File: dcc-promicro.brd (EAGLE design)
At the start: 33 x 17.8 mm, 7 parts, among them Q1 MOSFET-NCHANNEL2N7002PW

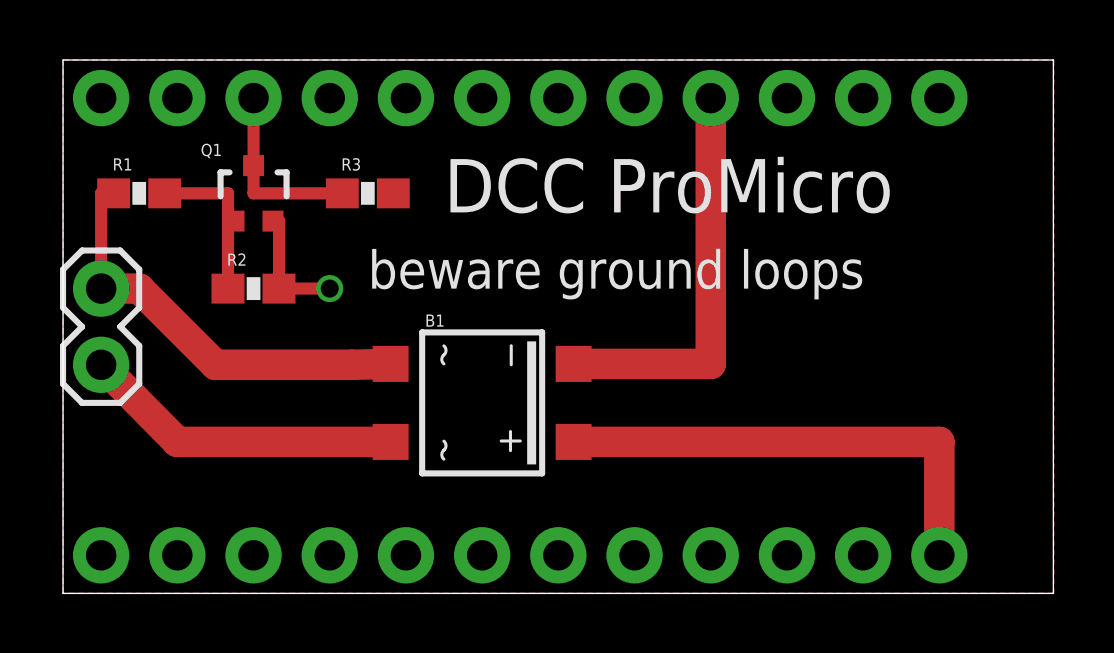
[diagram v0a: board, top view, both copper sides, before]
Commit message: add a-star variant, use JST for dcc-powered boards
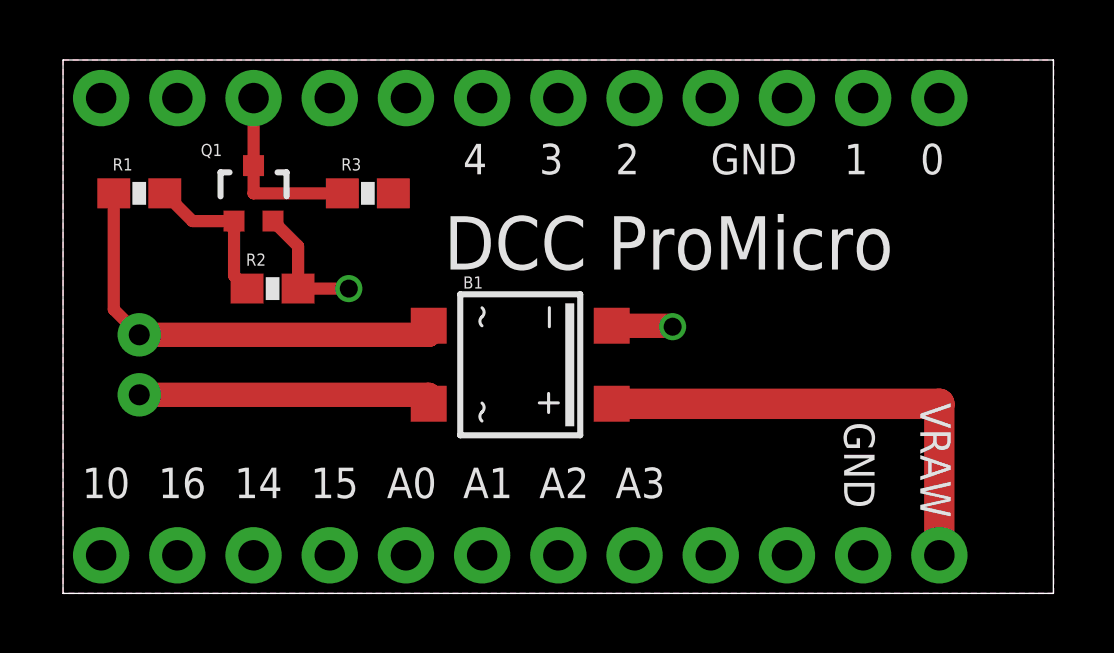
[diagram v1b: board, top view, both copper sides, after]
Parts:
- DCC-IN: value M02PTH -> M02-JST-2-PTH-NO_SILK; device SparkFun-Connectors:1X02 -> SparkFun-Connectors:JST-2-PTH-NS
- moved B1 1.80 mm to (15.2, 7.62)
- moved DCC-IN 1.27 mm to (2.54, 7.62)
- moved R2 0.64 mm to (6.99, 10.2)
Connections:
- net GND: now also U$1.23
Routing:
- net GND: track 17.6 -> 6.35 mm, vias 1 -> 2
- net N$4: track 10.8 -> 9.95 mm
- net N$3: track 14.3 -> 15.0 mm
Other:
- board text added: "0"
- board text added: "1"
- board text added: "10"
- board text added: "14"
- board text added: "15"
- board text added: "16"
- board text added: "2"
- board text added: "3"
- board text added: "4"
- board text added: "A0"
- board text added: "A1"
- board text added: "A2"
- board text added: "A3"
- board text added: "GND"
- board text added: "VRAW"
- board text removed: "beware ground loops"
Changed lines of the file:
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@@
 <layers>
 <layer number="1" name="Top" color="4" fill="1" visible="yes" active="yes"/>
+<layer number="2" name="Route2" color="1" fill="3" visible="no" active="no"/>
+<layer number="3" name="Route3" color="4" fill="3" visible="no" active="no"/>
+<layer number="14" name="Route14" color="1" fill="6" visible="no" active="no"/>
+<layer number="15" name="Route15" color="4" fill="6" visible="no" active="no"/>
 <layer number="16" name="Bottom" color="1" fill="1" visible="yes" active="yes"/>
 <layer number="17" name="Pads" color="2" fill="1" visible="yes" active="yes"/>
@@
 <wire x1="33.01" y1="0" x2="33.01" y2="17.78" width="0" layer="20"/>
 <wire x1="33.01" y1="17.78" x2="0" y2="17.78" width="0" layer="20"/>
-<text x="12.7" y="12.7" size="1.778" layer="21" font="vector">DCC ProMicro</text>
-<text x="10.16" y="10.16" size="1.27" layer="21" font="vector">beware ground loops</text>
+<text x="12.7" y="10.795" size="1.778" layer="21" font="vector">DCC ProMicro</text>
+<text x="13.335" y="13.97" size="1.016" layer="21">4</text>
+<text x="18.415" y="13.97" size="1.016" layer="21">2</text>
+<text x="15.875" y="13.97" size="1.016" layer="21">3</text>
+<text x="0.635" y="3.175" size="1.016" layer="21" rot="SR0">10</text>
+<text x="3.175" y="3.175" size="1.016" layer="21">16</text>
+<text x="5.715" y="3.175" size="1.016" layer="21">14</text>
+<text x="8.255" y="3.175" size="1.016" layer="21">15</text>
+<text x="26.035" y="13.97" size="1.016" layer="21">1</text>
+<text x="28.575" y="13.97" size="1.016" layer="21">0</text>
+<text x="21.59" y="13.97" size="1.016" layer="21">GND</text>
+<text x="28.575" y="6.35" size="1.016" layer="21" rot="SR270">VRAW</text>
+<text x="10.795" y="3.175" size="1.016" layer="21">A0</text>
+<text x="13.335" y="3.175" size="1.016" layer="21">A1</text>
+<text x="15.875" y="3.175" size="1.016" layer="21" rot="SR0">A2</text>
+<text x="18.415" y="3.175" size="1.016" layer="21" rot="SR0">A3</text>
+<text x="26.035" y="5.715" size="1.016" layer="21" rot="SR270">GND</text>
 </plain>
 <attributes>
@@
 </autorouter>
 <elements>
-<element name="DCC-IN" library="SparkFun-Connectors" package="1X02" value="M02PTH" x="1.27" y="7.62" smashed="yes" rot="R90"/>
+<element name="DCC-IN" library="SparkFun-Connectors" package="JST-2-PTH-NS" value="M02-JST-2-PTH-NO_SILK" x="2.54" y="7.62" smashed="yes" rot="R90"/>
 <element name="U$1" library="SparkFun-Boards" package="ARDUINO_PRO_MICRO" value="ARDUINO_PRO_MICRO" x="16.51" y="8.89" smashed="yes" rot="R270"/>
-<element name="B1" library="rectifier" package="SOIC-4" value="MB1S" x="13.97" y="6.35" smashed="yes" rot="R270">
-<attribute name="NAME" x="12.065" y="8.89" size="0.4064" layer="25"/>
+<element name="B1" library="rectifier" package="SOIC-4" value="MB1S" x="15.24" y="7.62" smashed="yes" rot="R270">
+<attribute name="NAME" x="13.335" y="10.16" size="0.4064" layer="25"/>
 </element>
 <element name="R1" library="SparkFun-Passives" package="0603-RES" value="47K" x="2.54" y="13.335"/>
@@
 </element>
 <element name="R3" library="SparkFun-Passives" package="0603-RES" value="10K" x="10.16" y="13.335"/>
-<element name="R2" library="SparkFun-Passives" package="0603-RES" value="100K" x="6.35" y="10.16"/>
+<element name="R2" library="SparkFun-Passives" package="0603-RES" value="100K" x="6.985" y="10.16"/>
 </elements>
 <signals>
@@
 <contactref element="B1" pad="-"/>
 <contactref element="Q1" pad="2"/>
-<wire x1="21.59" y1="16.51" x2="21.59" y2="7.65" width="1.016" layer="1"/>
-<wire x1="21.59" y1="7.65" x2="17.02" y2="7.65" width="1.016" layer="1"/>
 <contactref element="R2" pad="2"/>
-<wire x1="7.2" y1="10.16" x2="7.2" y2="12.41" width="0.4064" layer="1"/>
-<wire x1="7.2" y1="12.41" x2="7" y2="12.41" width="0.4064" layer="1"/>
-<wire x1="7.2" y1="10.16" x2="8.89" y2="10.16" width="0.4064" layer="1"/>
-<via x="8.89" y="10.16" extent="1-16" drill="0.6" shape="square"/>
+<wire x1="7.835" y1="10.16" x2="9.525" y2="10.16" width="0.4064" layer="1"/>
+<via x="9.525" y="10.16" extent="1-16" drill="0.6" shape="square"/>
+<contactref element="U$1" pad="23"/>
+<wire x1="18.29" y1="8.92" x2="20.32" y2="8.92" width="0.8128" layer="1"/>
+<wire x1="20.32" y1="8.92" x2="20.32" y2="8.89" width="0.8128" layer="1"/>
+<via x="20.32" y="8.89" extent="1-16" drill="0.6" shape="square"/>
+<wire x1="7.835" y1="10.16" x2="7.835" y2="11.575" width="0.4064" layer="1"/>
+<wire x1="7.835" y1="11.575" x2="7" y2="12.41" width="0.4064" layer="1"/>
 </signal>
 <signal name="DCC-INT">
@@
 <contactref element="U$1" pad="24"/>
 <contactref element="B1" pad="+"/>
-<wire x1="17.02" y1="5.05" x2="29.21" y2="5.05" width="1.016" layer="1"/>
-<wire x1="29.21" y1="5.05" x2="29.21" y2="1.27" width="1.016" layer="1"/>
+<wire x1="18.29" y1="6.32" x2="29.21" y2="6.32" width="1.016" layer="1"/>
+<wire x1="29.21" y1="6.32" x2="29.21" y2="1.27" width="1.016" layer="1"/>
 </signal>
 <signal name="N$3">
@@
 <contactref element="DCC-IN" pad="2"/>
 <contactref element="R1" pad="1"/>
-<wire x1="1.27" y1="10.16" x2="2.54" y2="10.16" width="1.016" layer="1"/>
-<wire x1="2.54" y1="10.16" x2="5.08" y2="7.62" width="1.016" layer="1"/>
-<wire x1="5.08" y1="7.62" x2="9.62" y2="7.62" width="1.016" layer="1"/>
-<wire x1="9.62" y1="7.62" x2="10.92" y2="7.65" width="1.016" layer="1"/>
-<wire x1="1.27" y1="10.16" x2="1.27" y2="13.335" width="0.4064" layer="1"/>
-<wire x1="1.27" y1="13.335" x2="1.69" y2="13.335" width="0.4064" layer="1"/>
+<wire x1="2.54" y1="8.62" x2="1.69" y2="9.47" width="0.4064" layer="1"/>
+<wire x1="1.69" y1="9.47" x2="1.69" y2="13.335" width="0.4064" layer="1"/>
+<wire x1="2.54" y1="8.62" x2="12.19" y2="8.62" width="0.8128" layer="1"/>
+<wire x1="12.19" y1="8.62" x2="12.19" y2="8.92" width="0.8128" layer="1"/>
 </signal>
 <signal name="N$4">
 <contactref element="B1" pad="~2"/>
 <contactref element="DCC-IN" pad="1"/>
-<wire x1="1.27" y1="7.62" x2="1.27" y2="7.59" width="0.4064" layer="1"/>
-<wire x1="1.27" y1="7.62" x2="3.81" y2="5.05" width="1.016" layer="1"/>
-<wire x1="3.81" y1="5.05" x2="10.92" y2="5.05" width="1.016" layer="1"/>
+<wire x1="2.54" y1="6.62" x2="12.19" y2="6.62" width="0.8128" layer="1"/>
+<wire x1="12.19" y1="6.62" x2="12.19" y2="6.32" width="0.8128" layer="1"/>
 </signal>
 <signal name="N$1">
@@
 <contactref element="Q1" pad="1"/>
 <contactref element="R2" pad="1"/>
-<wire x1="3.39" y1="13.335" x2="5.5" y2="13.335" width="0.4064" layer="1"/>
-<wire x1="5.5" y1="13.335" x2="5.5" y2="12.41" width="0.4064" layer="1"/>
-<wire x1="5.5" y1="12.41" x2="5.5" y2="10.16" width="0.4064" layer="1"/>
-<wire x1="5.7" y1="12.41" x2="5.5" y2="12.41" width="0.4064" layer="1"/>
+<wire x1="3.39" y1="13.335" x2="4.315" y2="12.41" width="0.4064" layer="1"/>
+<wire x1="4.315" y1="12.41" x2="5.7" y2="12.41" width="0.4064" layer="1"/>
+<wire x1="6.135" y1="10.16" x2="5.7" y2="10.595" width="0.4064" layer="1"/>
+<wire x1="5.7" y1="10.595" x2="5.7" y2="12.41" width="0.4064" layer="1"/>
 </signal>
 </signals>
